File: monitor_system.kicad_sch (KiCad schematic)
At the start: 0 parts

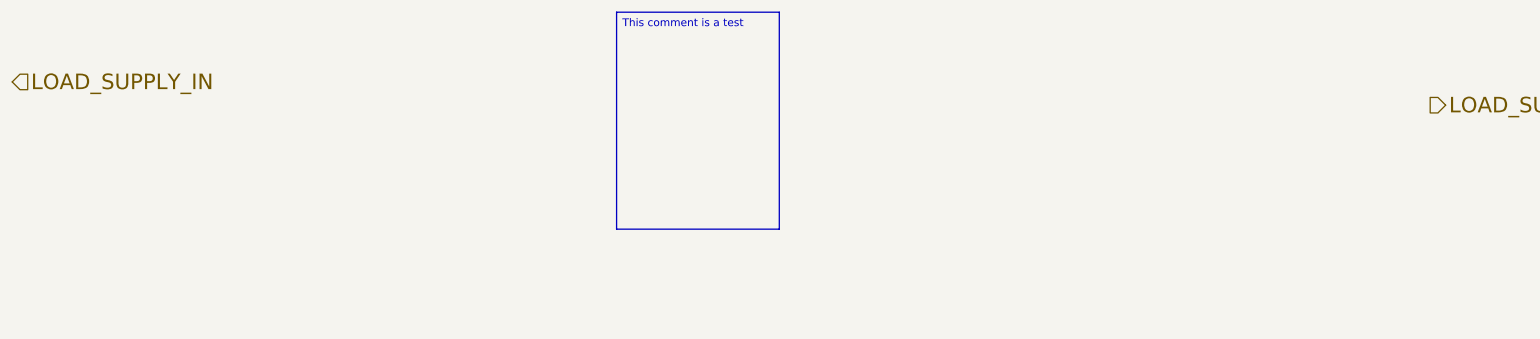
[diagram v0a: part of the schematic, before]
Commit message: feat:added relay to the monitor system
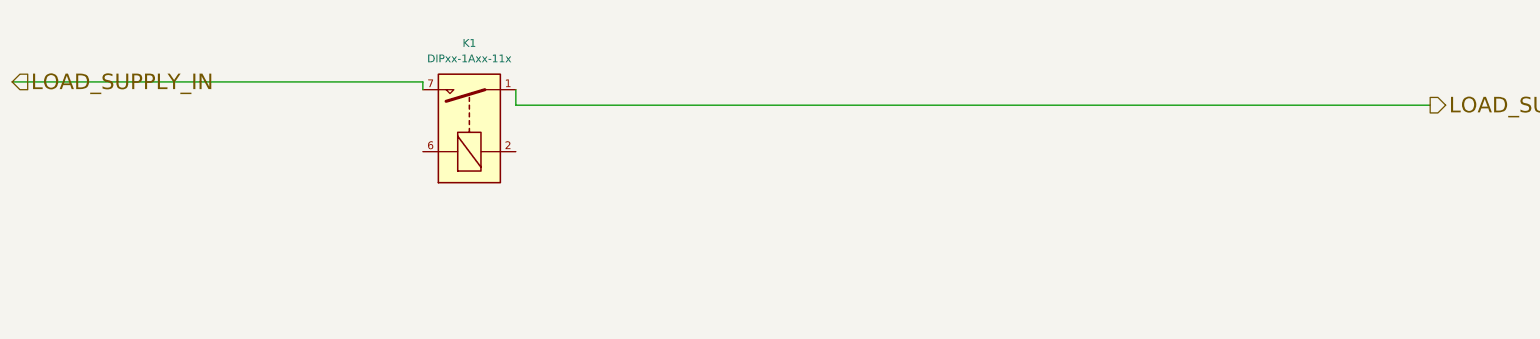
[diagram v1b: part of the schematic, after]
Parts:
- added K1: DIPxx-1Axx-11x, Relay_THT:Relay_StandexMeder_DIP_LowProfile, symbol Relay:DIPxx-1Axx-11x
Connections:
- net LOAD_SUPPLY_IN: now also K1.7, K1.8
- net LOAD_SUPPLY_OUT: now also K1.1, K1.14
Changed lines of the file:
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@@
 		)
 	)
-	(text_box "This comment is a test \n"
-		(exclude_from_sim no)
-		(at 113.03 22.86 0)
-		(size 26.67 35.56)
-		(margins 0.9525 0.9525 0.9525 0.9525)
+	(wire
+		(pts
+			(xy 81.28 34.29) (xy 81.28 35.56)
+		)
 		(stroke
 			(width 0)
-			(type solid)
+			(type default)
 		)
-		(fill
-			(type none)
+	)
+	(wire
+		(pts
+			(xy 13.97 34.29) (xy 81.28 34.29)
 		)
-		(effects
-			(font
-				(size 1.27 1.27)
-			)
-			(justify left top)
+		(stroke
+			(width 0)
+			(type default)
+		)
+	)
+	(wire
+		(pts
+			(xy 96.52 38.1) (xy 96.52 35.56)
+		)
+		(stroke
+			(width 0)
+			(type default)
+		)
+	)
+	(wire
+		(pts
+			(xy 246.38 38.1) (xy 96.52 38.1)
+		)
+		(stroke
+			(width 0)
+			(type default)
 		)
 	)
@@
 		)
 	)
+	(symbol
+		(lib_id "Relay:DIPxx-1Axx-11x")
+		(at 88.9 40.64 90)
+		(unit 1)
+		(exclude_from_sim no)
+		(in_bom yes)
+		(on_board yes)
+		(dnp no)
+		(fields_autoplaced yes)
+		(property "Reference" "K1"
+			(at 88.9 27.94 90)
+			(effects
+				(font
+					(size 1.27 1.27)
+				)
+			)
+		)
+		(property "Value" "DIPxx-1Axx-11x"
+			(at 88.9 30.48 90)
+			(effects
+				(font
+					(size 1.27 1.27)
+				)
+			)
+		)
+		(property "Footprint" "Relay_THT:Relay_StandexMeder_DIP_LowProfile"
+			(at 90.17 31.75 0)
+			(effects
+				(font
+					(size 1.27 1.27)
+				)
+				(justify left)
+				(hide yes)
+			)
+		)
+		(property "Datasheet" "https://standexelectronics.com/wp-content/uploads/datasheet_reed_relay_DIP.pdf"
+			(at 88.9 40.64 0)
+			(effects
+				(font
+					(size 1.27 1.27)
+				)
+				(hide yes)
+			)
+		)
+		(property "Description" "Standex Meder DIP reed relay, SPST, Closing Contact"
+			(at 88.9 40.64 0)
+			(effects
+				(font
+					(size 1.27 1.27)
+				)
+				(hide yes)
+			)
+		)
+		(pin "2"
+		)
+		(pin "1"
+		)
+		(pin "14"
+		)
+		(pin "7"
+		)
+		(pin "8"
+		)
+		(pin "6"
+		)
+		(instances
+			(project ""
+				(path "/bdc7face-9f7c-4701-80bb-4cc144448db1/2e815cd5-1f7c-4969-a83e-2a8a8597c7a4"
+					(reference "K1")
+					(unit 1)
+				)
+			)
+		)
+	)

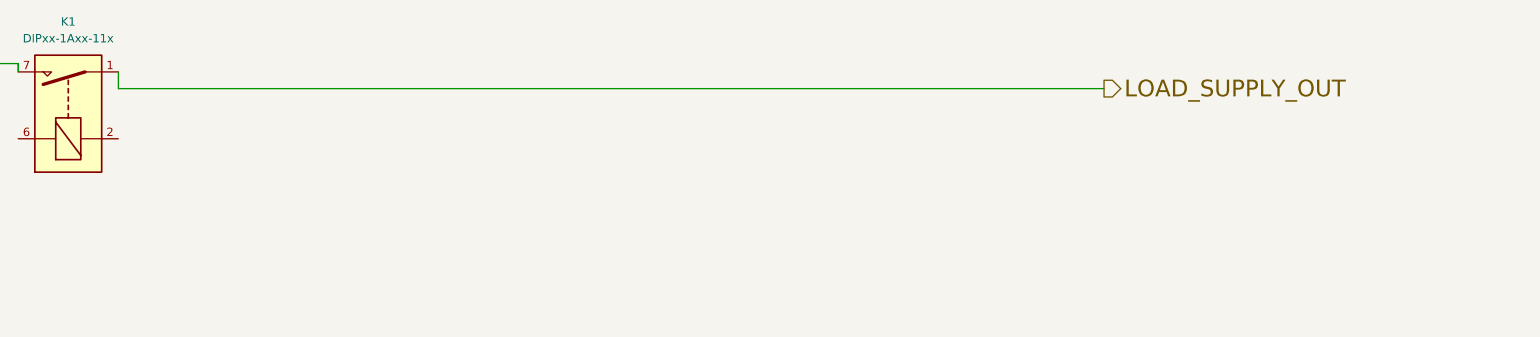
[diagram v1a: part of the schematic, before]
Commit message: feat: added hall sensor to the monitor system
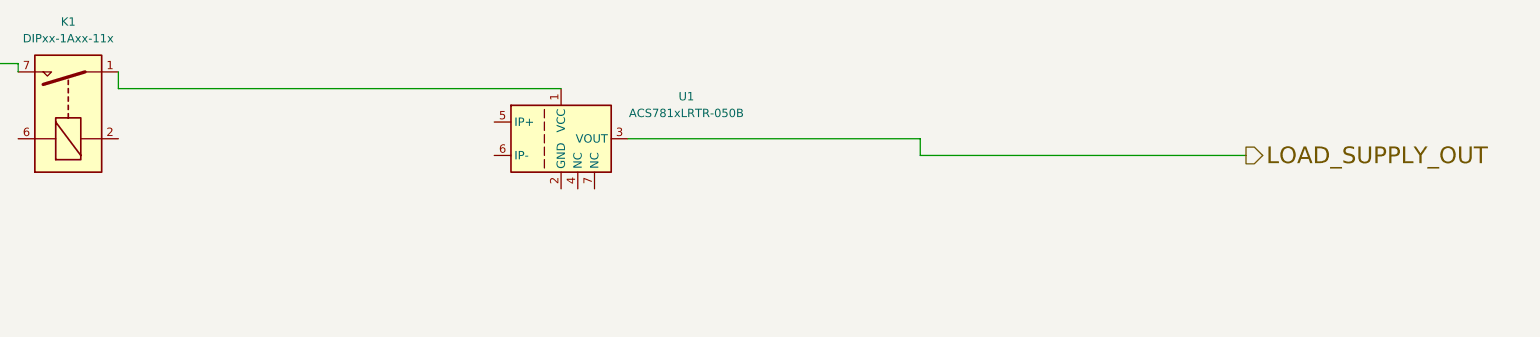
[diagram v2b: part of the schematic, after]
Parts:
- added U1: ACS781xLRTR-050B, Sensor_Current:Allegro_PSOF-7_4.8x6.4mm_P1.60mm, symbol Sensor_Current:ACS781xLRTR-050B
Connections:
- net LOAD_SUPPLY_OUT: now also U1.3 (VOUT); no longer K1.1, K1.14
- new net: K1.1, K1.14, U1.1 (VCC)
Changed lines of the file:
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@@
+	(wire
+		(pts
+			(xy 218.44 45.72) (xy 218.44 48.26)
+		)
+		(stroke
+			(width 0)
+			(type default)
+		)
+	)
+	(wire
+		(pts
+			(xy 218.44 48.26) (xy 267.97 48.26)
+		)
+		(stroke
+			(width 0)
+			(type default)
+		)
+	)
+	(wire
+		(pts
+			(xy 96.52 38.1) (xy 163.83 38.1)
+		)
+		(stroke
+			(width 0)
+			(type default)
+		)
+	)
 	(wire
 		(pts
@@
 	(wire
 		(pts
-			(xy 246.38 38.1) (xy 96.52 38.1)
+			(xy 173.99 45.72) (xy 218.44 45.72)
 		)
 		(stroke
@@
 	(hierarchical_label "LOAD_SUPPLY_OUT"
 		(shape output)
-		(at 246.38 38.1 0)
+		(at 267.97 48.26 0)
 		(effects
 			(font
@@
 					(unit 1)
 				)
+			)
+		)
+	)
+	(symbol
+		(lib_id "Sensor_Current:ACS781xLRTR-050B")
+		(at 163.83 45.72 0)
+		(unit 1)
+		(exclude_from_sim no)
+		(in_bom yes)
+		(on_board yes)
+		(dnp no)
+		(fields_autoplaced yes)
+		(property "Reference" "U1"
+			(at 182.88 39.2998 0)
+			(effects
+				(font
+					(size 1.27 1.27)
+				)
+			)
+		)
+		(property "Value" "ACS781xLRTR-050B"
+			(at 182.88 41.8398 0)
+			(effects
+				(font
+					(size 1.27 1.27)
+				)
+			)
+		)
+		(property "Footprint" "Sensor_Current:Allegro_PSOF-7_4.8x6.4mm_P1.60mm"
+			(at 163.83 45.72 0)
+			(effects
+				(font
+					(size 1.27 1.27)
+				)
+				(hide yes)
+			)
+		)
+		(property "Datasheet" "http://www.allegromicro.com/~/media/Files/Datasheets/ACS780-Datasheet.ashx?la=en"
+			(at 163.83 45.72 0)
+			(effects
+				(font
+					(size 1.27 1.27)
+				)
+				(hide yes)
+			)
+		)
+		(property "Description" "±50A Bidirectional Hall-Effect Current Sensor, +3.3V supply, 26.4mV/A, PSOF-7"
+			(at 163.83 45.72 0)
+			(effects
+				(font
+					(size 1.27 1.27)
+				)
+				(hide yes)
+			)
+		)
+		(pin "6"
+		)
+		(pin "2"
+		)
+		(pin "5"
+		)
+		(pin "4"
+		)
+		(pin "7"
+		)
+		(pin "3"
+		)
+		(pin "1"
+		)
+		(instances
+			(project ""
+				(path "/bdc7face-9f7c-4701-80bb-4cc144448db1/2e815cd5-1f7c-4969-a83e-2a8a8597c7a4"
+					(reference "U1")
+					(unit 1)
+				)

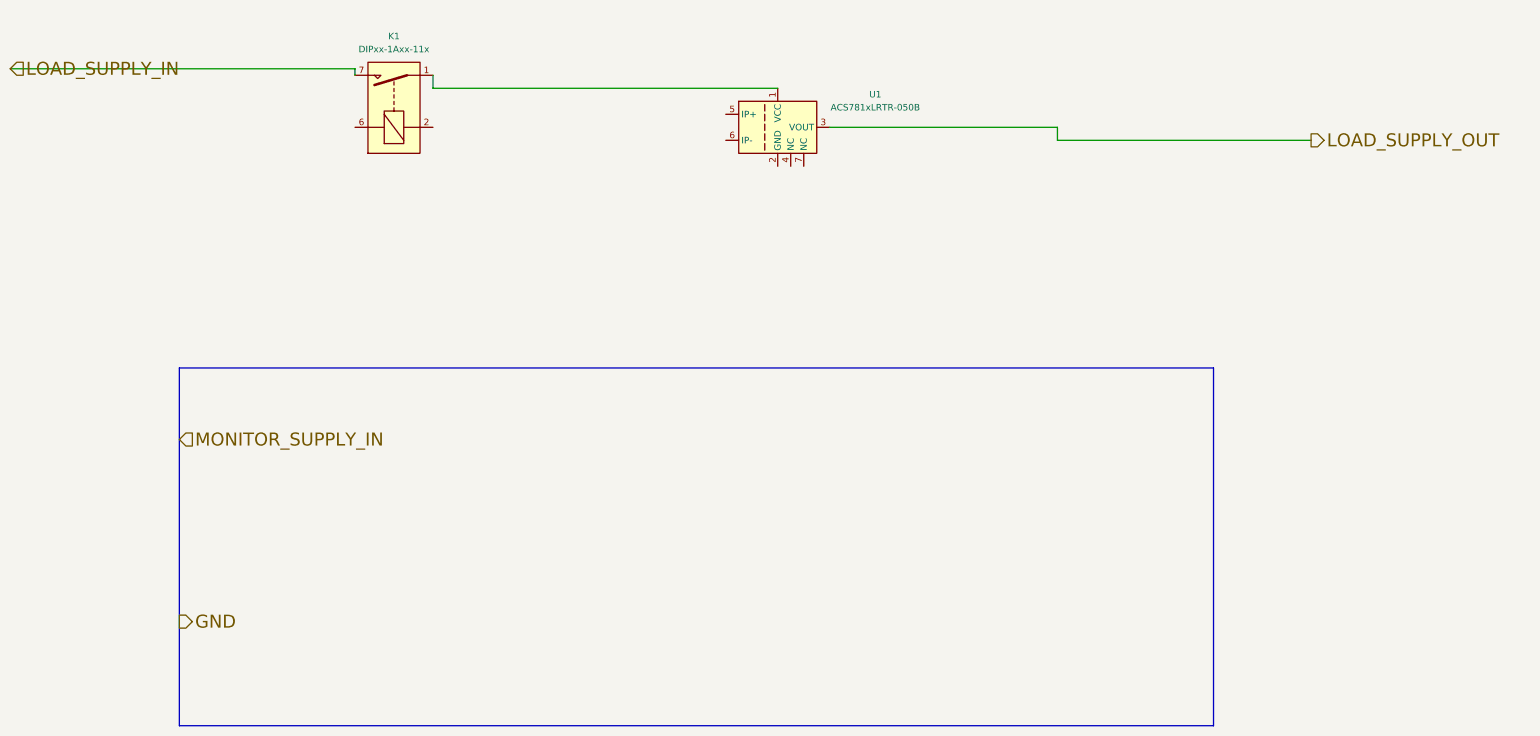
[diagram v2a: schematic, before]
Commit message: fix:fixed hall sensor connections
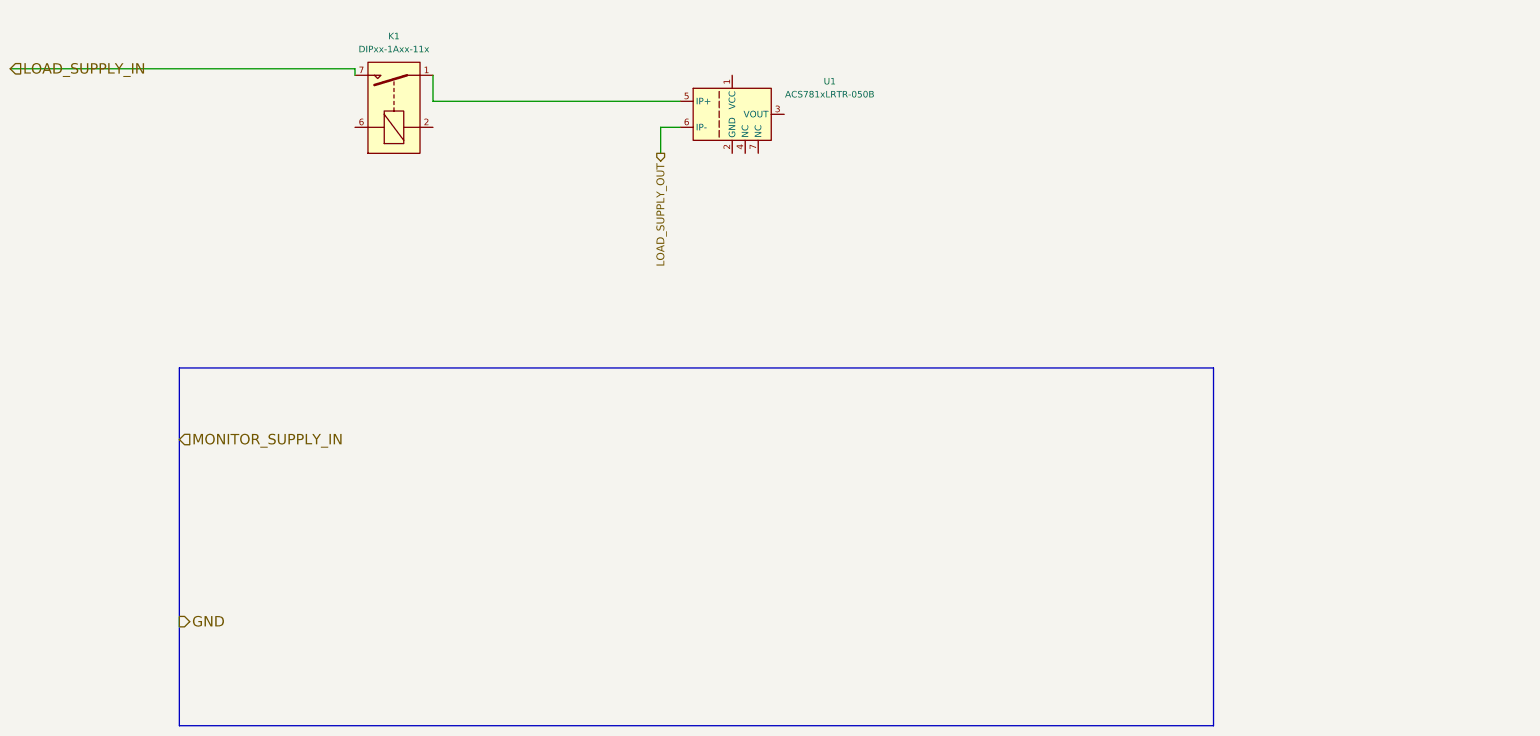
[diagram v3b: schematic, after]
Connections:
- net LOAD_SUPPLY_OUT: now also U1.6 (IP-); no longer U1.3 (VOUT)
- net at K1.1, K1.14: now also U1.5 (IP+); no longer U1.1 (VCC)
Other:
- moved on the sheet: U1
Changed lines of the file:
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@@
 	(wire
 		(pts
-			(xy 218.44 45.72) (xy 218.44 48.26)
+			(xy 144.78 45.72) (xy 140.97 45.72)
 		)
 		(stroke
@@
 	(wire
 		(pts
-			(xy 218.44 48.26) (xy 267.97 48.26)
+			(xy 140.97 45.72) (xy 140.97 50.8)
 		)
 		(stroke
@@
 	(wire
 		(pts
-			(xy 96.52 38.1) (xy 163.83 38.1)
+			(xy 96.52 40.64) (xy 96.52 35.56)
 		)
 		(stroke
@@
 	(wire
 		(pts
-			(xy 96.52 38.1) (xy 96.52 35.56)
-		)
-		(stroke
-			(width 0)
-			(type default)
-		)
-	)
-	(wire
-		(pts
-			(xy 173.99 45.72) (xy 218.44 45.72)
+			(xy 96.52 40.64) (xy 144.78 40.64)
 		)
 		(stroke
@@
 		(effects
 			(font
-				(size 2.54 2.54)
+				(size 2.032 2.032)
 			)
 			(justify left)
@@
 		(effects
 			(font
-				(size 2.54 2.54)
+				(size 2.032 2.032)
 			)
 			(justify left)
@@
 	(hierarchical_label "LOAD_SUPPLY_OUT"
 		(shape output)
-		(at 267.97 48.26 0)
+		(at 140.97 50.8 270)
 		(effects
 			(font
-				(size 2.54 2.54)
+				(size 1.524 1.524)
 			)
-			(justify left)
+			(justify right)
 		)
 	)
@@
 		(effects
 			(font
-				(size 2.54 2.54)
+				(size 2.032 2.032)
 			)
 			(justify left)
@@
 	(symbol
 		(lib_id "Sensor_Current:ACS781xLRTR-050B")
-		(at 163.83 45.72 0)
+		(at 154.94 43.18 0)
 		(unit 1)
 		(exclude_from_sim no)
@@
 		(fields_autoplaced yes)
 		(property "Reference" "U1"
-			(at 182.88 39.2998 0)
+			(at 173.99 36.7598 0)
 			(effects
 				(font
@@
 		)
 		(property "Value" "ACS781xLRTR-050B"
-			(at 182.88 41.8398 0)
+			(at 173.99 39.2998 0)
 			(effects
 				(font
@@
 		)
 		(property "Footprint" "Sensor_Current:Allegro_PSOF-7_4.8x6.4mm_P1.60mm"
-			(at 163.83 45.72 0)
+			(at 154.94 43.18 0)
 			(effects
 				(font
@@
 		)
 		(property "Datasheet" "http://www.allegromicro.com/~/media/Files/Datasheets/ACS780-Datasheet.ashx?la=en"
-			(at 163.83 45.72 0)
+			(at 154.94 43.18 0)
 			(effects
 				(font
@@
 		)
 		(property "Description" "±50A Bidirectional Hall-Effect Current Sensor, +3.3V supply, 26.4mV/A, PSOF-7"
-			(at 163.83 45.72 0)
+			(at 154.94 43.18 0)
 			(effects
 				(font
